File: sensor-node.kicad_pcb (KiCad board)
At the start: 2 copper layers, 63.5 x 63.5 mm, 51 parts, among them J1 DIGITAL_IN, J11 ANALOG_IN, J12 +5, J2 DIGITAL_OUT, J3 +24, J4 GND, J5 CANH_TERM, J6 CANL_TERM, J7 RJ45_A, J8 CORTEX_DEBUG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

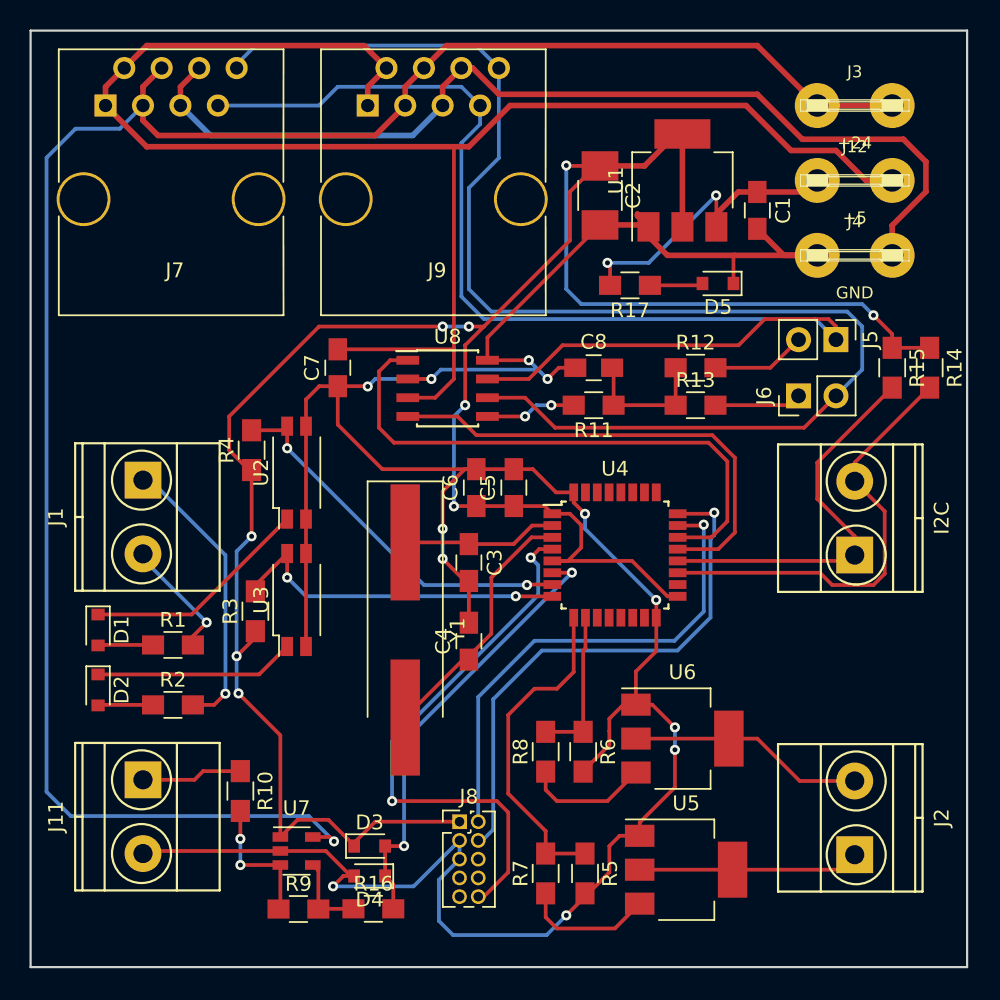
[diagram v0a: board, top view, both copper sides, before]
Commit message: Layout chaged for better routing on  the CAN differential
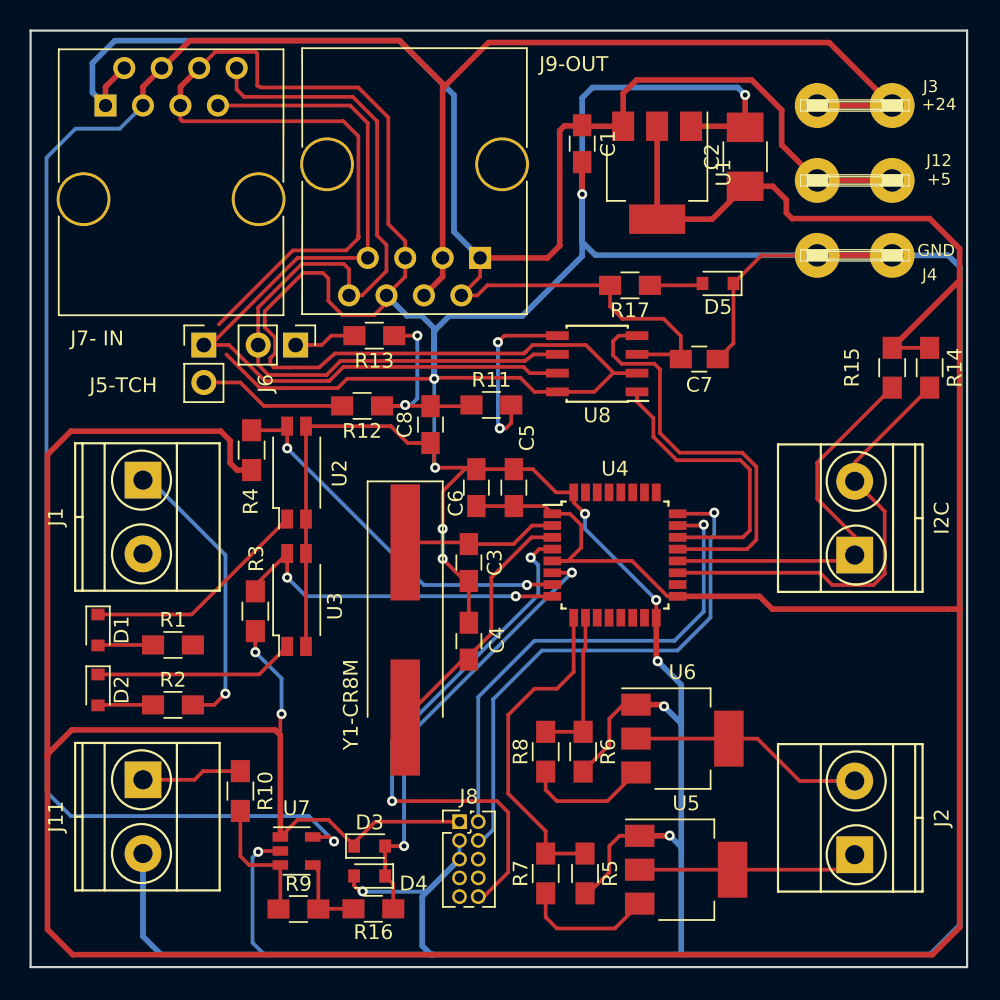
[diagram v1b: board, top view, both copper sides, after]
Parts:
- J7- IN: renamed from J7
- moved J5-TCH 42.9 mm to (62.5, 46.7), turned to 0 degrees
- moved J6 34.3 mm to (68.8, 46.7), turned to 270 degrees
- moved C7 24.5 mm to (96.1, 47.7), turned to 180 degrees
- moved R12 22.8 mm to (73.3, 50.8), turned to 180 degrees
- moved R13 22.3 mm to (74.1, 46.1), turned to 180 degrees
- moved J9-OUT 12.8 mm to (81.3, 40.8), turned to 180 degrees
- moved C1 12.7 mm to (88.2, 33.1)
- moved C8 11.7 mm to (77.9, 52.1), turned to 90 degrees
- moved U8 10.3 mm to (89.2, 48.0), turned to 180 degrees
- moved C2 10.2 mm to (99.3, 34.0), turned to 90 degrees
- moved R11 6.94 mm to (82.0, 50.8), turned to 0 degrees
- moved U1 1.79 mm to (93.3, 35.0), turned to 270 degrees
- renumbered J5 to J5-TCH, J9 to J9-OUT, Y1 to Y1-CR8M
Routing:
- net GND: track 265.7 -> 479.9 mm, vias 12 -> 13
- net +3V3: track 167.6 -> 297.6 mm, vias 9 -> 2
- net CANL: track 93.5 -> 59.8 mm
- net CANH: track 85.6 -> 58.9 mm
- net Net-(U4-Pad22): track 38.9 -> 20.2 mm
- net +5V: track 132.1 -> 113.8 mm, vias 2 -> 1
- net +24V: track 133.7 -> 151.2 mm
- net Net-(J1-Pad2): track 8.35 -> 0.33 mm, vias 1 -> 0
- net Net-(R11-Pad2): track 6.17 -> 12.3 mm
- net Net-(C8-Pad2): track 9.47 -> 14.5 mm, vias 0 -> 2
- net Net-(U4-Pad21): track 32.8 -> 28.7 mm
- net Net-(J5-Pad2): track 6.42 -> 10.0 mm
- net Net-(J6-Pad1): track 5.90 -> 4.25 mm
- net Net-(R10-Pad2): track 9.42 -> 9.06 mm, vias 2 -> 0

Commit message: Adding voltage divider/unity gain analog front end
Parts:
- J7: renamed from J7- IN
- R10: value 250K -> 22K
- R9: value 7K -> 11K
- moved C6 18.2 mm to (97.0, 65.1), turned to 270 degrees
- moved C5 17.9 mm to (99.2, 65.1), turned to 270 degrees
- moved R10 8.77 mm to (63.1, 85.5), turned to 0 degrees
- moved R9 0.75 mm to (68.5, 85.5)
- moved R16 0.63 mm to (73.8, 85.5)
- renumbered I2C to J10, J5-TCH to J5, J9-OUT to J9, Y1-CR8M to Y1
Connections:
- R9 pad 2: Net-(R16-Pad1) -> GND
- U7 pad 1: +3V3 -> Net-(R10-Pad2)
- U7 pad 3: Net-(R10-Pad2) -> Net-(R16-Pad1)
- U7 pad 5: +24V -> +5V
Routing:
- net +24V: track 151.2 -> 77.8 mm, vias 1 -> 0
- net +5V: track 113.8 -> 185.3 mm, vias 1 -> 2
- net +3V3: track 297.6 -> 272.3 mm
- net GND: track 479.9 -> 488.0 mm, vias 13 -> 14
- net Net-(J1-Pad2): track 0.33 -> 8.12 mm, vias 0 -> 1
- net Net-(J11-Pad1): track 6.85 -> 11.7 mm
- net Net-(R10-Pad2): track 9.06 -> 12.0 mm
- net Net-(R16-Pad1): track 5.53 -> 6.78 mm

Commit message: Update
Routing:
- net +3V3: track 272.3 -> 267.7 mm
- net GND: track 488.0 -> 486.7 mm
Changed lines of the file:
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@@
     (thickness 1.6)
     (drawings 4)
-    (tracks 557)
+    (tracks 561)
     (zones 0)
     (modules 51)
@@
   )
   (setup
-    (last_trace_width 0.254)
+    (last_trace_width 0.381)
     (user_trace_width 0.254)
     (user_trace_width 0.381)
@@
   (segment (start 55.88 30.48) (end 55.88 29.21) (width 0.381) (layer F.Cu) (net 1))
   (segment (start 55.88 29.21) (end 57.15 27.94) (width 0.381) (layer F.Cu) (net 1))
+  (segment (start 109.22 40.64) (end 111.713 40.64) (width 0.381) (layer B.Cu) (net 2))
+  (segment (start 113.157 86.661) (end 111.7727 88.0453) (width 0.381) (layer B.Cu) (net 2))
+  (segment (start 113.157 42.084) (end 113.157 86.661) (width 0.381) (layer B.Cu) (net 2))
+  (segment (start 111.713 40.64) (end 113.157 42.084) (width 0.381) (layer B.Cu) (net 2))
   (segment (start 78.74 59.182) (end 78.74 55.546) (width 0.254) (layer F.Cu) (net 2))
   (segment (start 78.74 61.214) (end 78.74 59.182) (width 0.254) (layer B.Cu) (net 2))
@@
   (via (at 94.1324 79.9808) (size 0.6858) (drill 0.3302) (layers F.Cu B.Cu) (net 2))
   (segment (start 94.9198 80.7682) (end 94.1324 79.9808) (width 0.381) (layer B.Cu) (net 2))
-  (segment (start 109.22 40.64) (end 113.0211 40.64) (width 0.381) (layer B.Cu) (net 2))
   (segment (start 77.3557 84.1083) (end 79.883 81.581) (width 0.381) (layer B.Cu) (net 2))
   (segment (start 94.9198 88.0453) (end 78.0923 88.0453) (width 0.381) (layer B.Cu) (net 2))
@@
   (segment (start 77.9399 88.0453) (end 77.3557 87.4611) (width 0.381) (layer B.Cu) (net 2))
   (segment (start 77.3557 87.4611) (end 77.3557 84.1083) (width 0.381) (layer B.Cu) (net 2))
-  (segment (start 111.8235 88.0453) (end 94.9198 88.0453) (width 0.381) (layer B.Cu) (net 2))
-  (segment (start 113.8047 86.0641) (end 111.8235 88.0453) (width 0.381) (layer B.Cu) (net 2))
-  (segment (start 113.8047 41.4236) (end 113.8047 86.0641) (width 0.381) (layer B.Cu) (net 2))
-  (segment (start 113.0211 40.64) (end 113.8047 41.4236) (width 0.381) (layer B.Cu) (net 2))
+  (segment (start 111.7727 88.0453) (end 94.9198 88.0453) (width 0.381) (layer B.Cu) (net 2))
   (segment (start 78.1685 49.0055) (end 78.1685 45.5892) (width 0.381) (layer B.Cu) (net 2))
   (segment (start 76.3143 44.7383) (end 74.93 43.354) (width 0.381) (layer B.Cu) (net 2))
@@
   (segment (start 63.326 26.844) (end 62.23 27.94) (width 0.254) (layer F.Cu) (net 2))
   (segment (start 60.96 29.21) (end 62.23 27.94) (width 0.381) (layer F.Cu) (net 2))
+  (segment (start 109.728 64.6265) (end 110.5535 64.6265) (width 0.381) (layer F.Cu) (net 3))
+  (segment (start 110.5535 64.6265) (end 113.157 67.23) (width 0.381) (layer F.Cu) (net 3))
   (segment (start 99.187 63.821) (end 100.2865 63.821) (width 0.381) (layer F.Cu) (net 3))
-  (segment (start 101.092 64.6265) (end 113.792 64.6265) (width 0.381) (layer F.Cu) (net 3))
   (segment (start 100.2865 63.821) (end 101.092 64.6265) (width 0.381) (layer F.Cu) (net 3))
+  (segment (start 101.092 64.6265) (end 109.728 64.6265) (width 0.381) (layer F.Cu) (net 3))
+  (segment (start 111.76 46.91) (end 111.76 46.275) (width 0.381) (layer F.Cu) (net 3))
+  (segment (start 111.76 46.275) (end 113.157 44.878) (width 0.381) (layer F.Cu) (net 3))
+  (segment (start 110.236 38.147) (end 110.744 38.147) (width 0.381) (layer F.Cu) (net 3))
+  (segment (start 113.157 86.788) (end 111.887 88.058) (width 0.381) (layer F.Cu) (net 3))
+  (segment (start 113.157 67.23) (end 113.157 86.788) (width 0.381) (layer F.Cu) (net 3))
+  (segment (start 113.157 40.56) (end 113.157 44.878) (width 0.381) (layer F.Cu) (net 3))
+  (segment (start 113.157 44.878) (end 113.157 67.23) (width 0.381) (layer F.Cu) (net 3))
+  (segment (start 110.744 38.147) (end 113.157 40.56) (width 0.381) (layer F.Cu) (net 3))
   (segment (start 97.028 63.821) (end 99.187 63.821) (width 0.381) (layer F.Cu) (net 3))
   (segment (start 94.674 63.76) (end 96.967 63.76) (width 0.381) (layer F.Cu) (net 3))
@@
   (via (at 65.913 68.246) (size 0.6858) (drill 0.3302) (layers F.Cu B.Cu) (net 3))
   (segment (start 65.913 68.246) (end 66.04 68.119) (width 0.254) (layer F.Cu) (net 3))
-  (segment (start 113.792 42.338) (end 113.792 64.6265) (width 0.381) (layer F.Cu) (net 3))
-  (segment (start 113.792 64.6265) (end 113.792 86.2165) (width 0.381) (layer F.Cu) (net 3))
   (segment (start 51.943 74.723) (end 51.943 72.4624) (width 0.381) (layer F.Cu) (net 3))
+  (segment (start 111.887 88.058) (end 53.6575 88.058) (width 0.381) (layer F.Cu) (net 3))
+  (segment (start 53.6575 88.058) (end 51.943 86.3435) (width 0.381) (layer F.Cu) (net 3))
   (segment (start 51.943 86.3435) (end 51.943 74.723) (width 0.381) (layer F.Cu) (net 3))
-  (segment (start 53.6575 88.058) (end 51.943 86.3435) (width 0.381) (layer F.Cu) (net 3))
-  (segment (start 111.9505 88.058) (end 53.6575 88.058) (width 0.381) (layer F.Cu) (net 3))
-  (segment (start 113.792 86.2165) (end 111.9505 88.058) (width 0.381) (layer F.Cu) (net 3))
   (segment (start 64.803 55.198) (end 65.786 55.198) (width 0.381) (layer F.Cu) (net 3))
   (segment (start 64.3255 54.7205) (end 64.803 55.198) (width 0.381) (layer F.Cu) (net 3))
@@
   (segment (start 51.943 72.4624) (end 51.943 54.149) (width 0.381) (layer F.Cu) (net 3))
   (segment (start 99.2505 35.956) (end 101.1235 35.956) (width 0.381) (layer F.Cu) (net 3))
-  (segment (start 113.792 42.338) (end 109.22 46.91) (width 0.381) (layer F.Cu) (net 3))
-  (segment (start 113.792 40.179) (end 113.792 42.338) (width 0.381) (layer F.Cu) (net 3))
-  (segment (start 111.76 38.147) (end 113.792 40.179) (width 0.381) (layer F.Cu) (net 3))
-  (segment (start 102.4255 38.147) (end 111.76 38.147) (width 0.381) (layer F.Cu) (net 3))
+  (segment (start 102.4255 38.147) (end 110.236 38.147) (width 0.381) (layer F.Cu) (net 3))
   (segment (start 102.0445 37.766) (end 102.4255 38.147) (width 0.381) (layer F.Cu) (net 3))
   (segment (start 102.0445 36.877) (end 102.0445 37.766) (width 0.381) (layer F.Cu) (net 3))

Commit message: Final Version
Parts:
- moved C3 6.34 mm to (75.1, 58.1), turned to 180 degrees
- moved C4 5.90 mm to (75.1, 69.2), turned to 180 degrees
- moved Y1 5.57 mm to (81.2, 63.7)
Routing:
- net Net-(C3-Pad1): track 11.0 -> 18.3 mm
- net (no net): track 0.00 -> 7.28 mm, vias 0 -> 2
- net GND: track 486.7 -> 480.5 mm, vias 14 -> 13
- net Net-(C4-Pad1): track 17.4 -> 18.4 mm
- net CANH: track 58.9 -> 59.4 mm
- added copper zone on B.Cu, net GND
- added copper zone on F.Cu, net GND

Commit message: Osh Park Ready
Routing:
- net (no net): track 7.28 -> 0.00 mm, vias 2 -> 0
- net GND: track 480.5 -> 483.5 mm, vias 13 -> 15
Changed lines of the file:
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@@
     (thickness 1.6)
     (drawings 4)
-    (tracks 590)
+    (tracks 584)
     (zones 0)
     (modules 51)
@@
   (layers
     (0 F.Cu signal)
-    (31 B.Cu signal)
+    (31 B.Cu signal hide)
     (32 B.Adhes user)
     (33 F.Adhes user)
@@
   )
   (setup
-    (last_trace_width 0.254)
+    (last_trace_width 0.381)
     (user_trace_width 0.254)
     (user_trace_width 0.381)
@@
   (gr_line (start 114.3 25.4) (end 114.3 88.9) (angle 90) (layer Edge.Cuts) (width 0.15))
   (gr_line (start 50.8 25.4) (end 114.3 25.4) (angle 90) (layer Edge.Cuts) (width 0.15))
-  (segment (start 110.1344 66.5569) (end 110.3503 66.5569) (width 0.381) (layer F.Cu) (net 0))
-  (segment (start 112.2045 60.8419) (end 111.8616 60.499) (width 0.381) (layer F.Cu) (net 0))
-  (segment (start 112.2045 61.7436) (end 112.2045 60.8419) (width 0.381) (layer F.Cu) (net 0))
-  (segment (start 112.3188 61.8579) (end 112.2045 61.7436) (width 0.381) (layer F.Cu) (net 0))
-  (via (at 112.3188 61.8579) (size 0.6858) (drill 0.3302) (layers F.Cu B.Cu) (net 0))
-  (segment (start 112.268 61.9087) (end 112.3188 61.8579) (width 0.381) (layer B.Cu) (net 0))
-  (segment (start 112.268 64.6392) (end 112.268 61.9087) (width 0.381) (layer B.Cu) (net 0))
-  (segment (start 110.3884 66.5188) (end 112.268 64.6392) (width 0.381) (layer B.Cu) (net 0))
-  (via (at 110.3884 66.5188) (size 0.6858) (drill 0.3302) (layers F.Cu B.Cu) (net 0))
-  (segment (start 110.3503 66.5569) (end 110.3884 66.5188) (width 0.381) (layer F.Cu) (net 0))
   (segment (start 55.88 30.48) (end 54.3014 30.48) (width 0.254) (layer B.Cu) (net 1))
   (segment (start 70.9358 80.076) (end 69.934 80.076) (width 0.254) (layer F.Cu) (net 1))
@@
   (segment (start 55.88 30.48) (end 55.88 29.21) (width 0.381) (layer F.Cu) (net 1))
   (segment (start 55.88 29.21) (end 57.15 27.94) (width 0.381) (layer F.Cu) (net 1))
+  (via (at 110.5789 67.1411) (size 0.6858) (drill 0.3302) (layers F.Cu B.Cu) (net 2))
+  (segment (start 110.5789 67.1411) (end 112.0902 65.6298) (width 0.381) (layer B.Cu) (net 2))
+  (segment (start 112.0902 65.6298) (end 112.0902 64.8043) (width 0.381) (layer B.Cu) (net 2))
+  (via (at 112.0902 64.8043) (size 0.6858) (drill 0.3302) (layers F.Cu B.Cu) (net 2))
   (segment (start 109.22 40.64) (end 111.713 40.64) (width 0.381) (layer B.Cu) (net 2))
   (segment (start 111.713 40.64) (end 113.2967 39.0563) (width 0.381) (layer B.Cu) (net 2))
